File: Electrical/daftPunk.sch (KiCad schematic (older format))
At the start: 18 parts, among them J1 Conn_01x03_Male, J2 Conn_01x03_Female

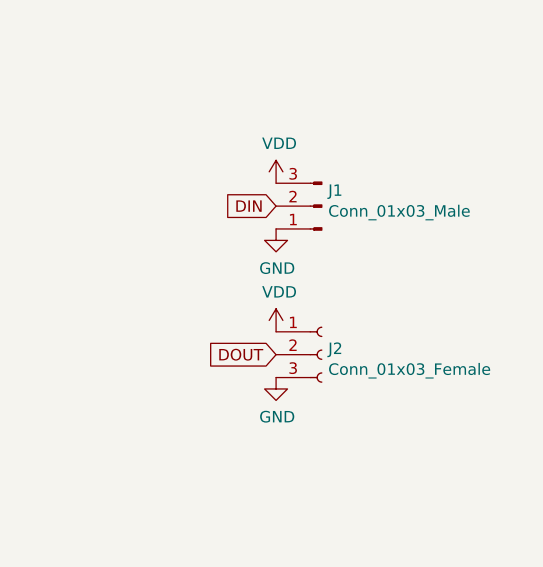
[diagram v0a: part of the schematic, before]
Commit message: PCB updated to only have pads for board interconnect
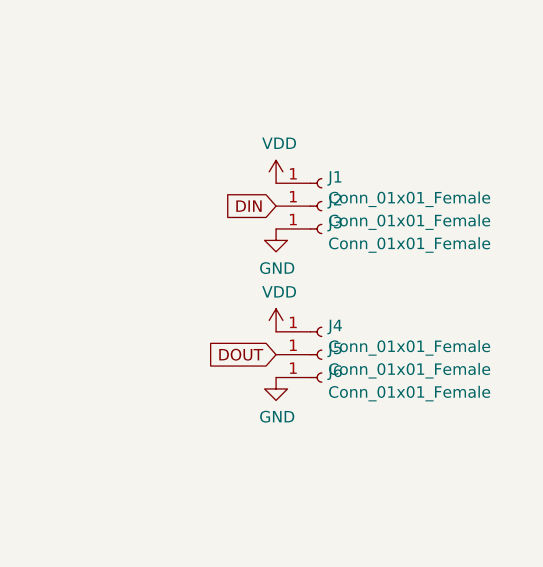
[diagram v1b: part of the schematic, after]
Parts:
- removed J1: Conn_01x03_Male, Connector_PinHeader_1.27mm:PinHeader_1x03_P1.27mm_Horizontal, symbol Connector:Conn_01x03_Male
- removed J2: Conn_01x03_Female, Connector_PinHeader_1.27mm:PinHeader_1x03_P1.27mm_Horizontal, symbol Connector:Conn_01x03_Female
- added J1, J2, J3, J4, J5, J6: Conn_01x01_Female, TestPoint:TestPoint_Pad_1.5x1.5mm, symbol Connector:Conn_01x01_Female
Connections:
- net DIN: now also J2.1 (Pin_1)
- net DOUT: now also J5.1 (Pin_1)
- net GND: now also J3.1 (Pin_1), J6.1 (Pin_1)
- net VDD: now also J1.1 (Pin_1), J4.1 (Pin_1)
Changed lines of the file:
@@
 	7350 3750 7350 3800
-$Comp
-L Connector:Conn_01x03_Male J1
-U 1 1 5F34A5CB
-P 9600 1700
-F 0 "J1" H 9572 1632 50  0000 R CNN
-F 1 "Conn_01x03_Male" H 9572 1723 50  0000 R CNN
-F 2 "Connector_PinHeader_1.27mm:PinHeader_1x03_P1.27mm_Horizontal" H 9600 1700 50  0001 C CNN
-F 3 "~" H 9600 1700 50  0001 C CNN
-	1    9600 1700
-	-1   0    0    1
-$EndComp
 $Comp
 L power:VDD #PWR01
@@
 Connection ~ 3150 1300
 $Comp
-L Connector:Conn_01x03_Female J2
-U 1 1 5F369F90
+L Connector:Conn_01x01_Female J4
+U 1 1 5F2CD6E3
+P 9600 2250
+F 0 "J4" H 9628 2276 50  0000 L CNN
+F 1 "Conn_01x01_Female" H 9628 2185 50  0000 L CNN
+F 2 "TestPoint:TestPoint_Pad_1.5x1.5mm" H 9600 2250 50  0001 C CNN
+F 3 "~" H 9600 2250 50  0001 C CNN
+	1    9600 2250
+	1    0    0    -1
+$EndComp
+$Comp
+L Connector:Conn_01x01_Female J5
+U 1 1 5F2CE02B
 P 9600 2350
-F 0 "J2" H 9628 2376 50  0000 L CNN
-F 1 "Conn_01x03_Female" H 9628 2285 50  0000 L CNN
-F 2 "Connector_PinHeader_1.27mm:PinHeader_1x03_P1.27mm_Horizontal" H 9600 2350 50  0001 C CNN
+F 0 "J5" H 9628 2376 50  0000 L CNN
+F 1 "Conn_01x01_Female" H 9628 2285 50  0000 L CNN
+F 2 "TestPoint:TestPoint_Pad_1.5x1.5mm" H 9600 2350 50  0001 C CNN
 F 3 "~" H 9600 2350 50  0001 C CNN
 	1    9600 2350
 	1    0    0    -1
 $EndComp
+$Comp
+L Connector:Conn_01x01_Female J6
+U 1 1 5F2CE722
+P 9600 2450
+F 0 "J6" H 9628 2476 50  0000 L CNN
+F 1 "Conn_01x01_Female" H 9628 2385 50  0000 L CNN
+F 2 "TestPoint:TestPoint_Pad_1.5x1.5mm" H 9600 2450 50  0001 C CNN
+F 3 "~" H 9600 2450 50  0001 C CNN
+	1    9600 2450
+	1    0    0    -1
+$EndComp
+$Comp
+L Connector:Conn_01x01_Female J1
+U 1 1 5F2D4083
+P 9600 1600
+F 0 "J1" H 9628 1626 50  0000 L CNN
+F 1 "Conn_01x01_Female" H 9628 1535 50  0000 L CNN
+F 2 "TestPoint:TestPoint_Pad_1.5x1.5mm" H 9600 1600 50  0001 C CNN
+F 3 "~" H 9600 1600 50  0001 C CNN
+	1    9600 1600
+	1    0    0    -1
+$EndComp
+$Comp
+L Connector:Conn_01x01_Female J2
+U 1 1 5F2D479E
+P 9600 1700
+F 0 "J2" H 9628 1726 50  0000 L CNN
+F 1 "Conn_01x01_Female" H 9628 1635 50  0000 L CNN
+F 2 "TestPoint:TestPoint_Pad_1.5x1.5mm" H 9600 1700 50  0001 C CNN
+F 3 "~" H 9600 1700 50  0001 C CNN
+	1    9600 1700
+	1    0    0    -1
+$EndComp
+$Comp
+L Connector:Conn_01x01_Female J3
+U 1 1 5F2D4F0D
+P 9600 1800
+F 0 "J3" H 9628 1826 50  0000 L CNN
+F 1 "Conn_01x01_Female" H 9628 1735 50  0000 L CNN
+F 2 "TestPoint:TestPoint_Pad_1.5x1.5mm" H 9600 1800 50  0001 C CNN
+F 3 "~" H 9600 1800 50  0001 C CNN
+	1    9600 1800
+	1    0    0    -1
+$EndComp
